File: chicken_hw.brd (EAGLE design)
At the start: 25.7 x 38.1 mm, 13 parts

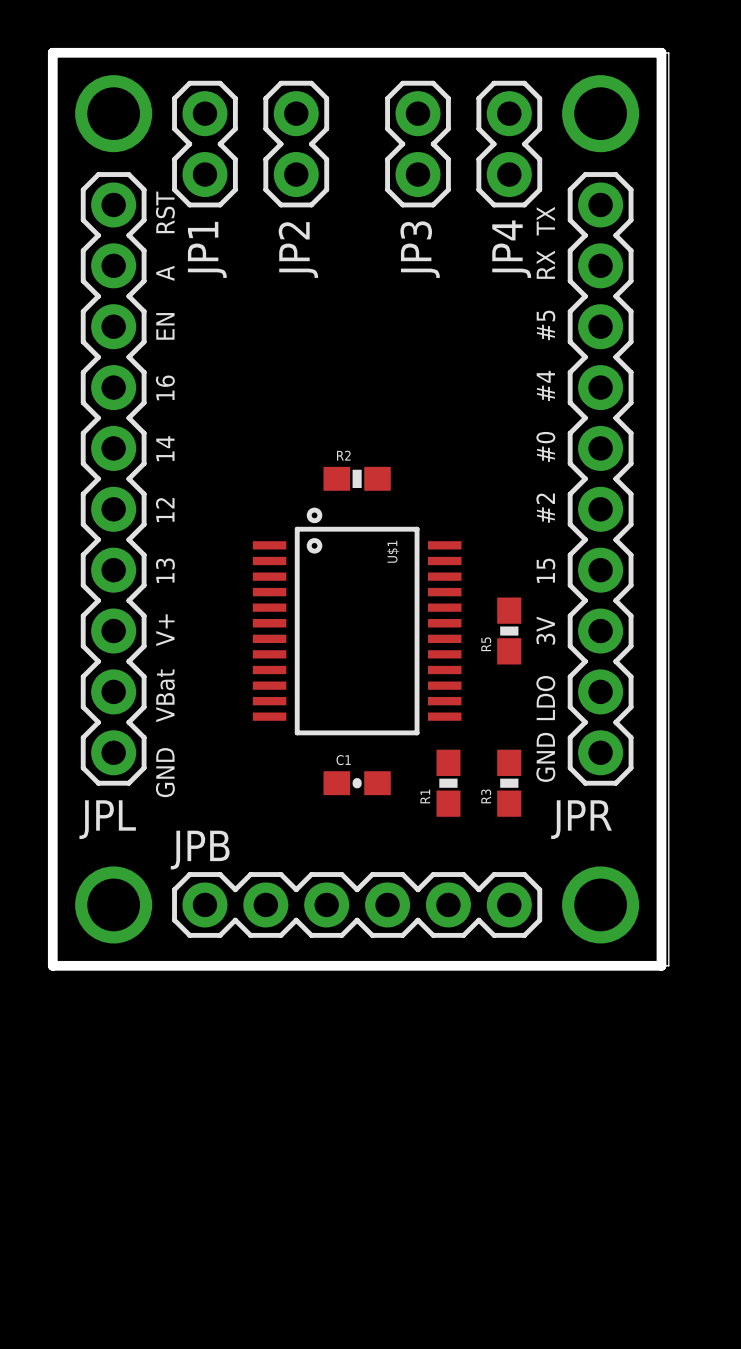
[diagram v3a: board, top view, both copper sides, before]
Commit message: Final initial placement of components, ready for autorouting
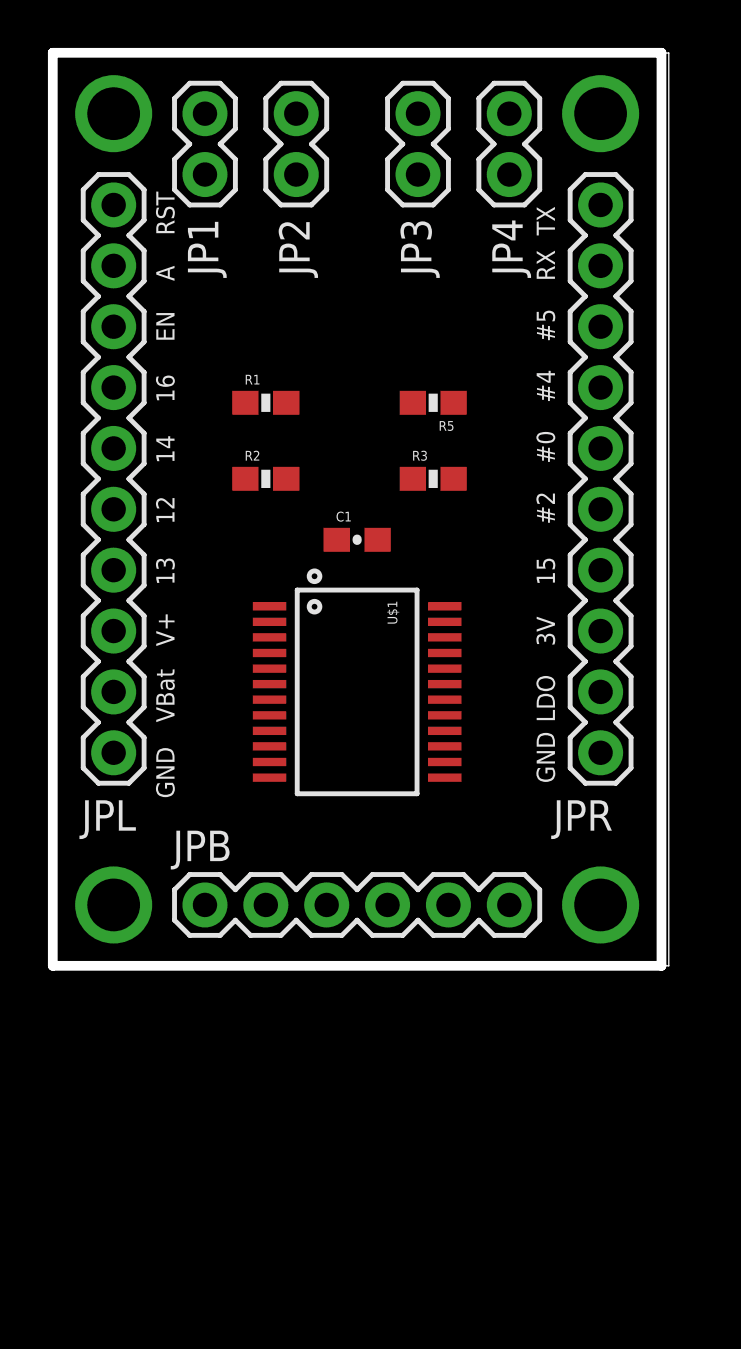
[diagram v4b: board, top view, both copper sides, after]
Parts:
- C1: value (none) -> 0.1uF
- moved R1 17.6 mm to (8.89, 23.5), turned to 0 degrees
- moved R3 13.1 mm to (15.9, 20.3), turned to 0 degrees
- moved C1 10.2 mm to (12.7, 17.8)
- moved R5 10.0 mm to (15.9, 23.5), turned to 180 degrees
- moved R2 3.81 mm to (8.89, 20.3)
- moved U$1 2.54 mm to (12.7, 11.4)
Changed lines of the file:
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@@
 <attribute name="VALUE" x="19.685" y="33.02" size="1.27" layer="27" rot="R270"/>
 </element>
-<element name="U$1" library="SparkFun-AnalogIC" package="SSOP24" value="MUX-74HC4067SMD" x="12.7" y="13.97" rot="R270">
-<attribute name="PROD_ID" value="IC-08252" x="12.7" y="13.97" size="1.778" layer="27" rot="R270" display="off"/>
+<element name="U$1" library="SparkFun-AnalogIC" package="SSOP24" value="MUX-74HC4067SMD" x="12.7" y="11.43" rot="R270">
+<attribute name="PROD_ID" value="IC-08252" x="12.7" y="11.43" size="1.778" layer="27" rot="R270" display="off"/>
 </element>
 <element name="JP1" library="SparkFun-Connectors" package="1X02" value="" x="6.35" y="35.56" smashed="yes" rot="R270">
@@
 <attribute name="VALUE" x="15.875" y="36.83" size="1.27" layer="27" rot="R270"/>
 </element>
-<element name="C1" library="SparkFun-Capacitors" package="0603-CAP" value="" x="12.7" y="7.62"/>
-<element name="R5" library="SparkFun-Resistors" package="0603-RES" value="10k" x="19.05" y="13.97" rot="R90"/>
-<element name="R1" library="SparkFun-Resistors" package="0603-RES" value="10k" x="16.51" y="7.62" rot="R90"/>
-<element name="R3" library="SparkFun-Resistors" package="0603-RES" value="10k" x="19.05" y="7.62" rot="R90"/>
-<element name="R2" library="SparkFun-Resistors" package="0603-RES" value="238k" x="12.7" y="20.32"/>
+<element name="C1" library="SparkFun-Capacitors" package="0603-CAP" value="0.1uF" x="12.7" y="17.78"/>
+<element name="R5" library="SparkFun-Resistors" package="0603-RES" value="10k" x="15.875" y="23.495" rot="R180"/>
+<element name="R1" library="SparkFun-Resistors" package="0603-RES" value="10k" x="8.89" y="23.495"/>
+<element name="R3" library="SparkFun-Resistors" package="0603-RES" value="10k" x="15.875" y="20.32"/>
+<element name="R2" library="SparkFun-Resistors" package="0603-RES" value="238k" x="8.89" y="20.32"/>
 </elements>
 <signals>
@@
 <contactref element="U$1" pad="1"/>
 <contactref element="R2" pad="1"/>
-<wire x1="9.044" y1="17.545" x2="11.85" y2="20.32" width="0" layer="19" extent="1-1"/>
-<wire x1="2.54" y1="29.21" x2="9.044" y2="17.545" width="0" layer="19" extent="1-1"/>
+<wire x1="9.044" y1="15.005" x2="8.04" y2="20.32" width="0" layer="19" extent="1-1"/>
+<wire x1="2.54" y1="29.21" x2="9.044" y2="15.005" width="0" layer="19" extent="1-1"/>
 </signal>
 <signal name="EN">
@@
 <contactref element="JPR" pad="4"/>
 <contactref element="U$1" pad="10"/>
-<wire x1="9.044" y1="11.695" x2="22.86" y2="24.13" width="0" layer="19" extent="1-1"/>
+<wire x1="9.044" y1="9.155" x2="22.86" y2="24.13" width="0" layer="19" extent="1-1"/>
 </signal>
 <signal name="GPIO5">
 <contactref element="JPR" pad="3"/>
 <contactref element="U$1" pad="11"/>
-<wire x1="9.044" y1="11.045" x2="22.86" y2="26.67" width="0" layer="19" extent="1-1"/>
+<wire x1="9.044" y1="8.505" x2="22.86" y2="26.67" width="0" layer="19" extent="1-1"/>
 </signal>
 <signal name="RX_R">
@@
 <contactref element="R5" pad="2"/>
 <contactref element="R2" pad="2"/>
-<wire x1="19.05" y1="14.82" x2="22.86" y2="13.97" width="0" layer="19" extent="1-1"/>
-<wire x1="16.356" y1="17.545" x2="19.05" y2="14.82" width="0" layer="19" extent="1-1"/>
-<wire x1="13.55" y1="20.32" x2="16.356" y2="17.545" width="0" layer="19" extent="1-1"/>
-<wire x1="11.85" y1="7.62" x2="19.05" y2="14.82" width="0" layer="19" extent="1-1"/>
+<wire x1="15.025" y1="23.495" x2="22.86" y2="13.97" width="0" layer="19" extent="1-1"/>
+<wire x1="16.356" y1="15.005" x2="15.025" y2="23.495" width="0" layer="19" extent="1-1"/>
+<wire x1="9.74" y1="20.32" x2="16.356" y2="15.005" width="0" layer="19" extent="1-1"/>
+<wire x1="11.85" y1="17.78" x2="15.025" y2="23.495" width="0" layer="19" extent="1-1"/>
 </signal>
 <signal name="EN_MUX">
@@
 <contactref element="JPR" pad="6"/>
 <contactref element="R5" pad="1"/>
-<wire x1="19.05" y1="13.12" x2="22.86" y2="19.05" width="0" layer="19" extent="1-1"/>
-<wire x1="16.356" y1="11.695" x2="19.05" y2="13.12" width="0" layer="19" extent="1-1"/>
+<wire x1="16.725" y1="23.495" x2="22.86" y2="19.05" width="0" layer="19" extent="1-1"/>
+<wire x1="16.356" y1="9.155" x2="16.725" y2="23.495" width="0" layer="19" extent="1-1"/>
 </signal>
 <signal name="N$2">
 <contactref element="JP1" pad="2"/>
 <contactref element="U$1" pad="9"/>
-<wire x1="9.044" y1="12.345" x2="6.35" y2="33.02" width="0" layer="19" extent="1-1"/>
+<wire x1="9.044" y1="9.805" x2="6.35" y2="33.02" width="0" layer="19" extent="1-1"/>
 </signal>
 <signal name="N$3">
 <contactref element="JP2" pad="2"/>
 <contactref element="U$1" pad="8"/>
-<wire x1="9.044" y1="12.995" x2="10.16" y2="33.02" width="0" layer="19" extent="1-1"/>
+<wire x1="9.044" y1="10.455" x2="10.16" y2="33.02" width="0" layer="19" extent="1-1"/>
 </signal>
 <signal name="N$4">
 <contactref element="JP3" pad="2"/>
 <contactref element="U$1" pad="7"/>
-<wire x1="9.044" y1="13.645" x2="15.24" y2="33.02" width="0" layer="19" extent="1-1"/>
+<wire x1="9.044" y1="11.105" x2="15.24" y2="33.02" width="0" layer="19" extent="1-1"/>
 </signal>
 <signal name="N$5">
 <contactref element="JP4" pad="2"/>
 <contactref element="U$1" pad="6"/>
-<wire x1="9.044" y1="14.295" x2="19.05" y2="33.02" width="0" layer="19" extent="1-1"/>
+<wire x1="9.044" y1="11.755" x2="19.05" y2="33.02" width="0" layer="19" extent="1-1"/>
 </signal>
 <signal name="N$1">
 <contactref element="U$1" pad="13"/>
 <contactref element="R1" pad="2"/>
-<wire x1="16.51" y1="8.47" x2="16.356" y2="10.395" width="0" layer="19" extent="1-1"/>
+<wire x1="9.74" y1="23.495" x2="16.356" y2="7.855" width="0" layer="19" extent="1-1"/>
 </signal>
 <signal name="N$6">
 <contactref element="U$1" pad="14"/>
 <contactref element="R3" pad="2"/>
-<wire x1="19.05" y1="8.47" x2="16.356" y2="11.045" width="0" layer="19" extent="1-1"/>
+<wire x1="16.725" y1="20.32" x2="16.356" y2="8.505" width="0" layer="19" extent="1-1"/>
 </signal>
 </signals>

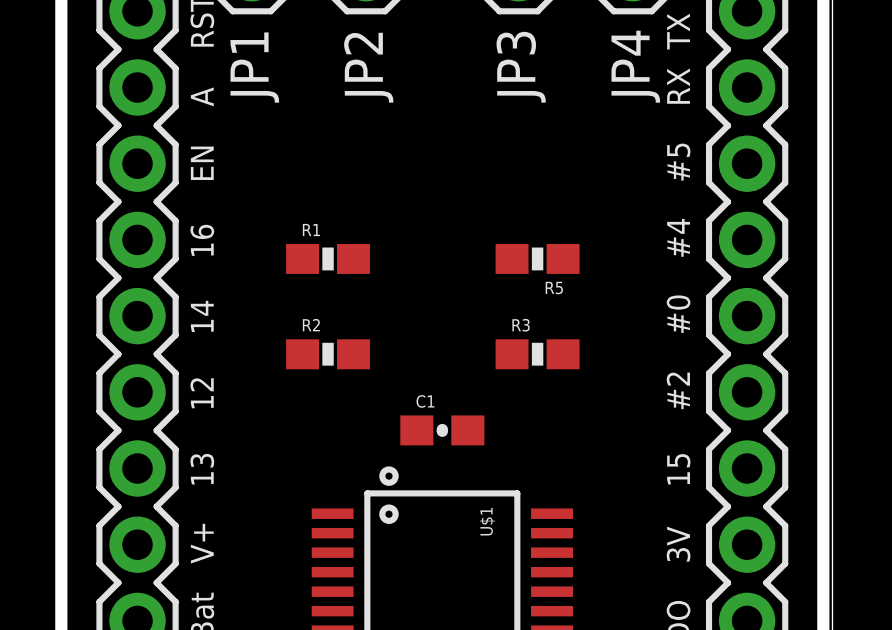
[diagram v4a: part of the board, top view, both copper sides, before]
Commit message: Improve lettering thickness on SMT parts
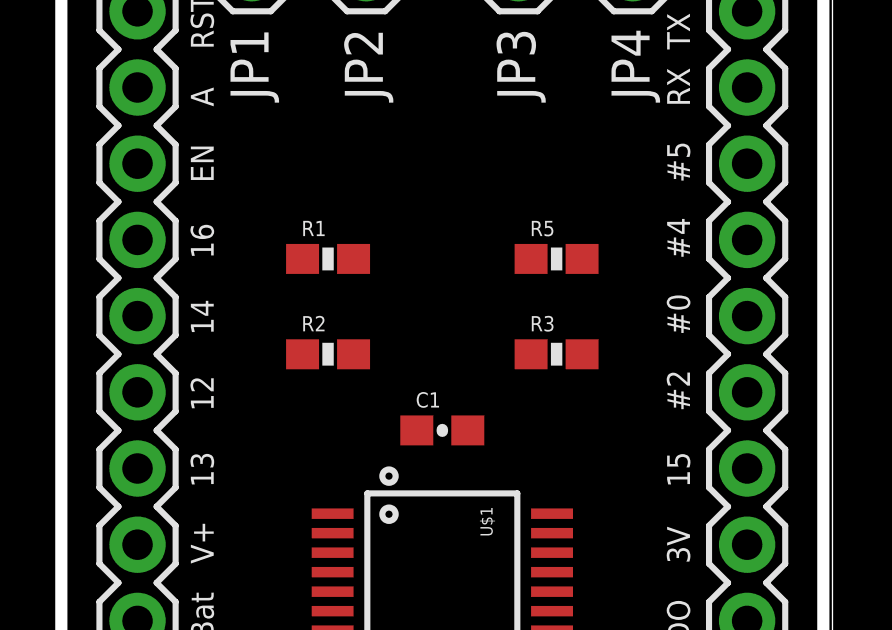
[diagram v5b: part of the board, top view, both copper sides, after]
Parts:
- moved R3 0.64 mm to (16.5, 20.3)
- moved R5 0.64 mm to (16.5, 23.5), turned to 0 degrees
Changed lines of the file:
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@@
 <attribute name="VALUE" x="15.875" y="36.83" size="1.27" layer="27" rot="R270"/>
 </element>
-<element name="C1" library="SparkFun-Capacitors" package="0603-CAP" value="0.1uF" x="12.7" y="17.78"/>
-<element name="R5" library="SparkFun-Resistors" package="0603-RES" value="10k" x="15.875" y="23.495" rot="R180"/>
-<element name="R1" library="SparkFun-Resistors" package="0603-RES" value="10k" x="8.89" y="23.495"/>
-<element name="R3" library="SparkFun-Resistors" package="0603-RES" value="10k" x="15.875" y="20.32"/>
-<element name="R2" library="SparkFun-Resistors" package="0603-RES" value="238k" x="8.89" y="20.32"/>
+<element name="C1" library="SparkFun-Capacitors" package="0603-CAP" value="0.1uF" x="12.7" y="17.78" smashed="yes">
+<attribute name="NAME" x="11.811" y="18.542" size="0.508" layer="25" font="vector" ratio="12"/>
+<attribute name="VALUE" x="11.684" y="16.637" size="0.508" layer="27" font="vector" ratio="12"/>
+</element>
+<element name="R5" library="SparkFun-Resistors" package="0603-RES" value="10k" x="16.51" y="23.495" smashed="yes">
+<attribute name="NAME" x="15.621" y="24.257" size="0.508" layer="25" font="vector"/>
+<attribute name="VALUE" x="15.494" y="22.098" size="0.508" layer="27" font="vector" ratio="12"/>
+</element>
+<element name="R1" library="SparkFun-Resistors" package="0603-RES" value="10k" x="8.89" y="23.495" smashed="yes">
+<attribute name="NAME" x="8.001" y="24.257" size="0.508" layer="25" font="vector" ratio="12"/>
+<attribute name="VALUE" x="7.874" y="22.098" size="0.508" layer="27" font="vector" ratio="12"/>
+</element>
+<element name="R3" library="SparkFun-Resistors" package="0603-RES" value="10k" x="16.51" y="20.32" smashed="yes">
+<attribute name="NAME" x="15.621" y="21.082" size="0.508" layer="25" font="vector" ratio="12"/>
+<attribute name="VALUE" x="15.494" y="18.923" size="0.508" layer="27" font="vector" ratio="12"/>
+</element>
+<element name="R2" library="SparkFun-Resistors" package="0603-RES" value="238k" x="8.89" y="20.32" smashed="yes">
+<attribute name="NAME" x="8.001" y="21.082" size="0.508" layer="25" font="vector" ratio="12"/>
+<attribute name="VALUE" x="7.874" y="18.923" size="0.508" layer="27" font="vector" ratio="12"/>
+</element>
 </elements>
 <signals>
@@
 <contactref element="R5" pad="2"/>
 <contactref element="R2" pad="2"/>
-<wire x1="15.025" y1="23.495" x2="22.86" y2="13.97" width="0" layer="19" extent="1-1"/>
-<wire x1="16.356" y1="15.005" x2="15.025" y2="23.495" width="0" layer="19" extent="1-1"/>
+<wire x1="17.36" y1="23.495" x2="22.86" y2="13.97" width="0" layer="19" extent="1-1"/>
+<wire x1="16.356" y1="15.005" x2="17.36" y2="23.495" width="0" layer="19" extent="1-1"/>
 <wire x1="9.74" y1="20.32" x2="16.356" y2="15.005" width="0" layer="19" extent="1-1"/>
-<wire x1="11.85" y1="17.78" x2="15.025" y2="23.495" width="0" layer="19" extent="1-1"/>
+<wire x1="11.85" y1="17.78" x2="17.36" y2="23.495" width="0" layer="19" extent="1-1"/>
 </signal>
 <signal name="EN_MUX">
@@
 <contactref element="JPR" pad="6"/>
 <contactref element="R5" pad="1"/>
-<wire x1="16.725" y1="23.495" x2="22.86" y2="19.05" width="0" layer="19" extent="1-1"/>
-<wire x1="16.356" y1="9.155" x2="16.725" y2="23.495" width="0" layer="19" extent="1-1"/>
+<wire x1="15.66" y1="23.495" x2="22.86" y2="19.05" width="0" layer="19" extent="1-1"/>
+<wire x1="16.356" y1="9.155" x2="15.66" y2="23.495" width="0" layer="19" extent="1-1"/>
 </signal>
 <signal name="N$2">
@@
 <contactref element="U$1" pad="14"/>
 <contactref element="R3" pad="2"/>
-<wire x1="16.725" y1="20.32" x2="16.356" y2="8.505" width="0" layer="19" extent="1-1"/>
+<wire x1="17.36" y1="20.32" x2="16.356" y2="8.505" width="0" layer="19" extent="1-1"/>
 </signal>
 </signals>
